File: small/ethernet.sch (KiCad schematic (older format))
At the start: 22 parts, among them J6 RJ45_Amphenol_RJMG1BD3B8K1ANR, U4 ENC28J60x-SS, Y1 Crystal

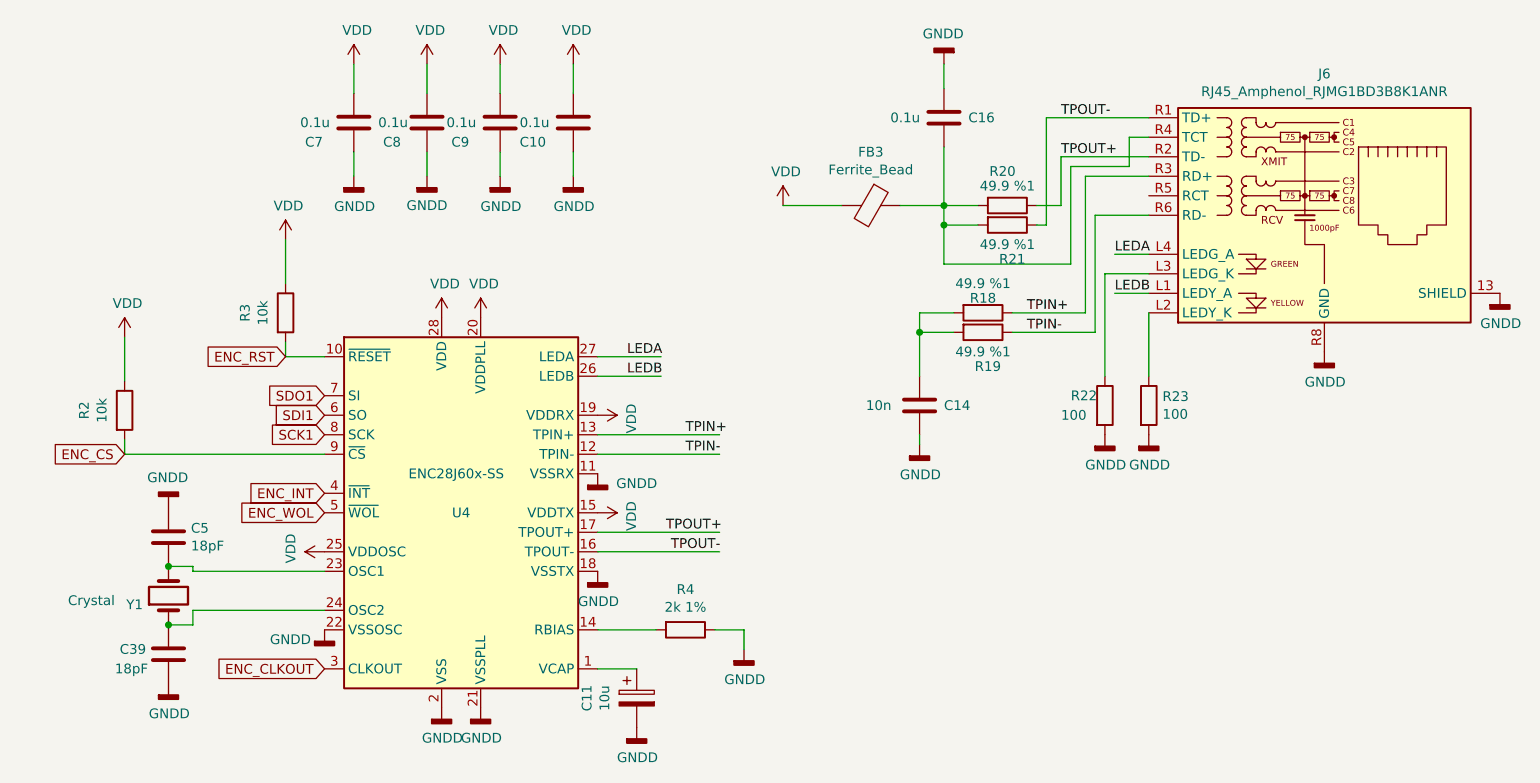
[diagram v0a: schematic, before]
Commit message: sim800 changed to sim808
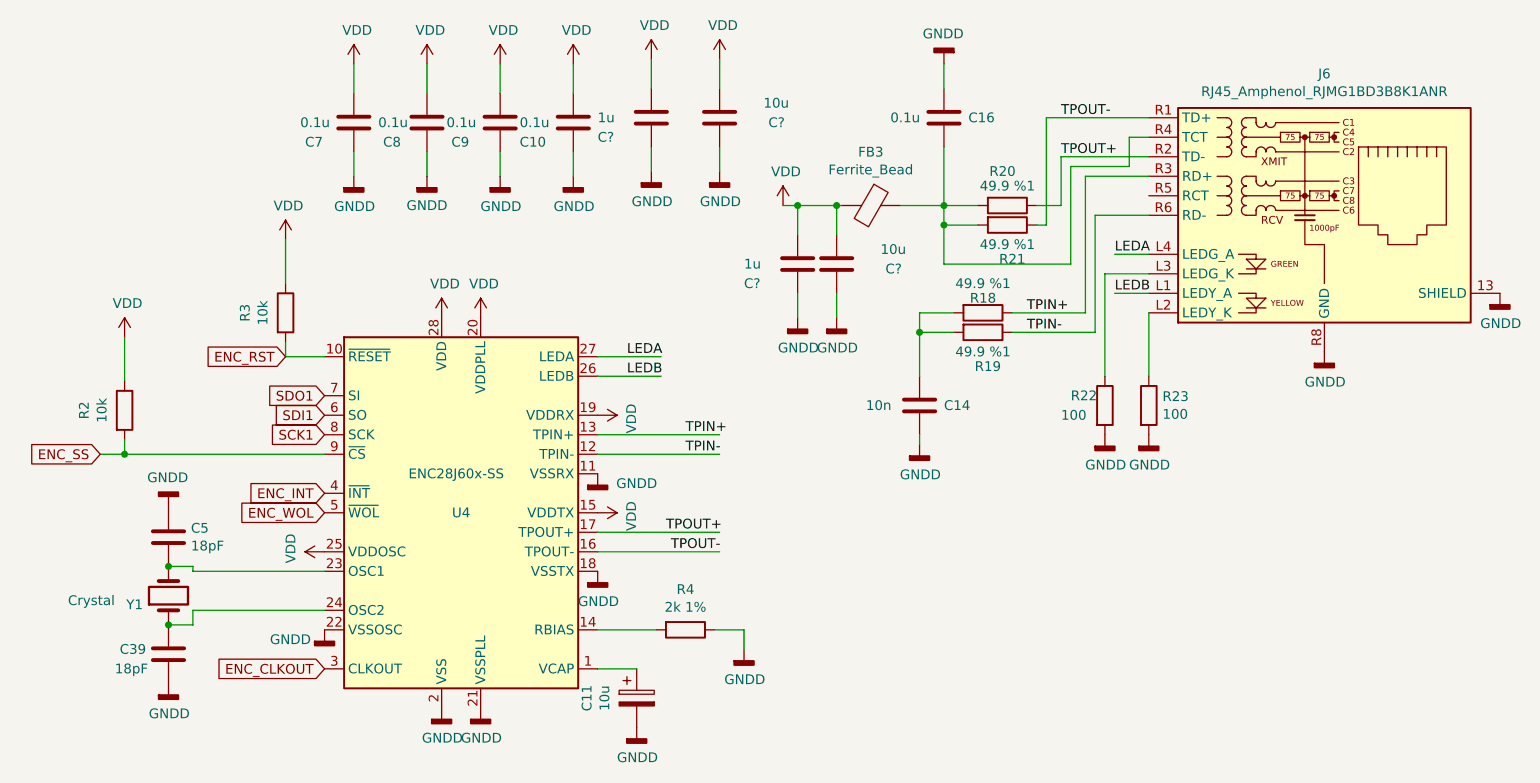
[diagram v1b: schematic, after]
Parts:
- added C? (x2): 1u, Capacitor_SMD:C_0603_1608Metric, symbol Device:C
- added C? (x2): 10u, Capacitor_SMD:C_0603_1608Metric, symbol Device:C
- R4: LCSC C22975 -> C22905; MPN 0603WAF2001T5E -> 0603WAF2321T5E
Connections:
- net labels added: ENC_SS
- net labels removed: ENC_CS
- wire segments 65 -> 76
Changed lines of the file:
@@
 $Descr A4 11693 8268
 encoding utf-8
-Sheet 6 8
+Sheet 6 9
 Title ""
 Date ""
@@
 	1    0    0    -1
 $EndComp
-Text GLabel 1625 2700 0    50   Input ~ 0
-ENC_CS
-Wire Wire Line
-	1625 2700 2650 2700
 Text GLabel 2650 2900 0    50   Input ~ 0
 ENC_INT
@@
 F 1 "2k 1%" V 4384 3600 50  0000 C CNN
 F 2 "Resistor_SMD:R_0603_1608Metric" V 4430 3600 50  0001 C CNN
-F 3 "https://datasheet.lcsc.com/szlcsc/Uniroyal-Elec-0603WAF2001T5E_C22975.pdf" H 4500 3600 50  0001 C CNN
-F 4 "C22975" V 4500 3600 50  0001 C CNN "LCSC"
-F 5 "0603WAF2001T5E" V 4500 3600 50  0001 C CNN "MPN"
+F 3 "https://datasheet.lcsc.com/szlcsc/Uniroyal-Elec-0603WAF2321T5E_C22905.pdf" H 4500 3600 50  0001 C CNN
+F 4 "C22905" V 4500 3600 50  0001 C CNN "LCSC"
+F 5 "0603WAF2321T5E" V 4500 3600 50  0001 C CNN "MPN"
 F 6 "0.0016" V 4500 3600 50  0001 C CNN "Price"
 	1    4500 3600
@@
 	1    0    0    -1
 $EndComp
-Wire Wire Line
-	5300 1425 5000 1425
 Connection ~ 5825 1525
 Wire Wire Line
@@
 $EndComp
 Connection ~ 1850 3575
+Text GLabel 1500 2700 0    50   Input ~ 0
+ENC_SS
+Wire Wire Line
+	1500 2700 1625 2700
+Connection ~ 1625 2700
+Wire Wire Line
+	1625 2700 2650 2700
+$Comp
+L power:GNDD #PWR?
+U 1 1 602BF6C6
+P 4325 1250
+AR Path="/602BF6C6" Ref="#PWR?"  Part="1"
+AR Path="/60757620/602BF6C6" Ref="#PWR?"  Part="1"
+F 0 "#PWR?" H 4325 1000 50  0001 C CNN
+F 1 "GNDD" H 4329 1095 50  0000 C CNN
+F 2 "" H 4325 1250 50  0001 C CNN
+F 3 "" H 4325 1250 50  0001 C CNN
+	1    4325 1250
+	1    0    0    -1
+$EndComp
+Wire Wire Line
+	4325 675  4325 825
+$Comp
+L power:VDD #PWR?
+U 1 1 602BF6CD
+P 4325 675
+AR Path="/602BF6CD" Ref="#PWR?"  Part="1"
+AR Path="/60757620/602BF6CD" Ref="#PWR?"  Part="1"
+F 0 "#PWR?" H 4325 525 50  0001 C CNN
+F 1 "VDD" H 4342 848 50  0000 C CNN
+F 2 "" H 4325 675 50  0001 C CNN
+F 3 "" H 4325 675 50  0001 C CNN
+	1    4325 675
+	1    0    0    -1
+$EndComp
+Wire Wire Line
+	4325 1250 4325 1125
+$Comp
+L Device:C C?
+U 1 1 602BF6D7
+P 4325 975
+AR Path="/602BF6D7" Ref="C?"  Part="1"
+AR Path="/6078415F/602BF6D7" Ref="C?"  Part="1"
+AR Path="/60757620/602BF6D7" Ref="C?"  Part="1"
+F 0 "C?" H 4050 875 50  0000 L CNN
+F 1 "1u" H 4050 975 50  0000 L CNN
+F 2 "Capacitor_SMD:C_0603_1608Metric" H 4363 825 50  0001 C CNN
+F 3 "https://datasheet.lcsc.com/szlcsc/Samsung-Electro-Mechanics-CL10A105KB8NNNC_C15849.pdf" H 4325 975 50  0001 C CNN
+F 4 "C15849" H 4325 975 50  0001 C CNN "LCSC"
+F 5 "0.0126" H 4325 975 50  0001 C CNN "Price"
+F 6 "CL10A105KB8NNNC" H 4325 975 50  0001 C CNN "MPN"
+	1    4325 975
+	1    0    0    -1
+$EndComp
+$Comp
+L power:GNDD #PWR?
+U 1 1 602C0E21
+P 4675 1250
+AR Path="/602C0E21" Ref="#PWR?"  Part="1"
+AR Path="/60757620/602C0E21" Ref="#PWR?"  Part="1"
+F 0 "#PWR?" H 4675 1000 50  0001 C CNN
+F 1 "GNDD" H 4679 1095 50  0000 C CNN
+F 2 "" H 4675 1250 50  0001 C CNN
+F 3 "" H 4675 1250 50  0001 C CNN
+	1    4675 1250
+	1    0    0    -1
+$EndComp
+Wire Wire Line
+	4675 675  4675 825
+$Comp
+L power:VDD #PWR?
+U 1 1 602C0E28
+P 4675 675
+AR Path="/602C0E28" Ref="#PWR?"  Part="1"
+AR Path="/60757620/602C0E28" Ref="#PWR?"  Part="1"
+F 0 "#PWR?" H 4675 525 50  0001 C CNN
+F 1 "VDD" H 4692 848 50  0000 C CNN
+F 2 "" H 4675 675 50  0001 C CNN
+F 3 "" H 4675 675 50  0001 C CNN
+	1    4675 675
+	1    0    0    -1
+$EndComp
+Wire Wire Line
+	4675 1250 4675 1125
+$Comp
+L Device:C C?
+U 1 1 602C0E32
+P 4675 975
+AR Path="/602C0E32" Ref="C?"  Part="1"
+AR Path="/6078415F/602C0E32" Ref="C?"  Part="1"
+AR Path="/60757620/602C0E32" Ref="C?"  Part="1"
+F 0 "C?" H 4925 950 50  0000 L CNN
+F 1 "10u" H 4900 1050 50  0000 L CNN
+F 2 "Capacitor_SMD:C_0603_1608Metric" H 4713 825 50  0001 C CNN
+F 3 "https://datasheet.lcsc.com/szlcsc/1912111437_Murata-Electronics-GRM188R61E106KA73D_C344022.pdf" H 4675 975 50  0001 C CNN
+F 4 "C344022" H 4675 975 50  0001 C CNN "LCSC"
+F 5 "0.0354" H 4675 975 50  0001 C CNN "Price"
+F 6 "GRM188R61E106KA73D" H 4675 975 50  0001 C CNN "MPN"
+	1    4675 975
+	1    0    0    -1
+$EndComp
+$Comp
+L power:GNDD #PWR?
+U 1 1 602CE763
+P 5075 2000
+AR Path="/602CE763" Ref="#PWR?"  Part="1"
+AR Path="/60757620/602CE763" Ref="#PWR?"  Part="1"
+F 0 "#PWR?" H 5075 1750 50  0001 C CNN
+F 1 "GNDD" H 5079 1845 50  0000 C CNN
+F 2 "" H 5075 2000 50  0001 C CNN
+F 3 "" H 5075 2000 50  0001 C CNN
+	1    5075 2000
+	1    0    0    -1
+$EndComp
+Wire Wire Line
+	5075 1425 5075 1575
+Wire Wire Line
+	5075 2000 5075 1875
+$Comp
+L Device:C C?
+U 1 1 602CE76E
+P 5075 1725
+AR Path="/602CE76E" Ref="C?"  Part="1"
+AR Path="/6078415F/602CE76E" Ref="C?"  Part="1"
+AR Path="/60757620/602CE76E" Ref="C?"  Part="1"
+F 0 "C?" H 4800 1625 50  0000 L CNN
+F 1 "1u" H 4800 1725 50  0000 L CNN
+F 2 "Capacitor_SMD:C_0603_1608Metric" H 5113 1575 50  0001 C CNN
+F 3 "https://datasheet.lcsc.com/szlcsc/Samsung-Electro-Mechanics-CL10A105KB8NNNC_C15849.pdf" H 5075 1725 50  0001 C CNN
+F 4 "C15849" H 5075 1725 50  0001 C CNN "LCSC"
+F 5 "0.0126" H 5075 1725 50  0001 C CNN "Price"
+F 6 "CL10A105KB8NNNC" H 5075 1725 50  0001 C CNN "MPN"
+	1    5075 1725
+	1    0    0    -1
+$EndComp
+$Comp
+L power:GNDD #PWR?
+U 1 1 602CE774
+P 5275 2000
+AR Path="/602CE774" Ref="#PWR?"  Part="1"
+AR Path="/60757620/602CE774" Ref="#PWR?"  Part="1"
+F 0 "#PWR?" H 5275 1750 50  0001 C CNN
+F 1 "GNDD" H 5279 1845 50  0000 C CNN
+F 2 "" H 5275 2000 50  0001 C CNN
+F 3 "" H 5275 2000 50  0001 C CNN
+	1    5275 2000
+	1    0    0    -1
+$EndComp
+Wire Wire Line
+	5275 1425 5275 1575
+Wire Wire Line
+	5275 2000 5275 1875
+$Comp
+L Device:C C?
+U 1 1 602CE77F
+P 5275 1725
+AR Path="/602CE77F" Ref="C?"  Part="1"
+AR Path="/6078415F/602CE77F" Ref="C?"  Part="1"
+AR Path="/60757620/602CE77F" Ref="C?"  Part="1"
+F 0 "C?" H 5525 1700 50  0000 L CNN
+F 1 "10u" H 5500 1800 50  0000 L CNN
+F 2 "Capacitor_SMD:C_0603_1608Metric" H 5313 1575 50  0001 C CNN
+F 3 "https://datasheet.lcsc.com/szlcsc/1912111437_Murata-Electronics-GRM188R61E106KA73D_C344022.pdf" H 5275 1725 50  0001 C CNN
+F 4 "C344022" H 5275 1725 50  0001 C CNN "LCSC"
+F 5 "0.0354" H 5275 1725 50  0001 C CNN "Price"
+F 6 "GRM188R61E106KA73D" H 5275 1725 50  0001 C CNN "MPN"
+	1    5275 1725
+	1    0    0    -1
+$EndComp
+Connection ~ 5075 1425
+Wire Wire Line
+	5075 1425 5000 1425
+Wire Wire Line
+	5075 1425 5275 1425
+Connection ~ 5275 1425
+Wire Wire Line
+	5275 1425 5300 1425
 $EndSCHEMATC

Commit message: simcard colder changed to 78800-0001
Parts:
- gave numbers to parts that had none: 4
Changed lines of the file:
@@
 P 4325 1250
 AR Path="/602BF6C6" Ref="#PWR?"  Part="1"
-AR Path="/60757620/602BF6C6" Ref="#PWR?"  Part="1"
-F 0 "#PWR?" H 4325 1000 50  0001 C CNN
+AR Path="/60757620/602BF6C6" Ref="#PWR0127"  Part="1"
+F 0 "#PWR0127" H 4325 1000 50  0001 C CNN
 F 1 "GNDD" H 4329 1095 50  0000 C CNN
 F 2 "" H 4325 1250 50  0001 C CNN
@@
 P 4325 675
 AR Path="/602BF6CD" Ref="#PWR?"  Part="1"
-AR Path="/60757620/602BF6CD" Ref="#PWR?"  Part="1"
-F 0 "#PWR?" H 4325 525 50  0001 C CNN
+AR Path="/60757620/602BF6CD" Ref="#PWR0130"  Part="1"
+F 0 "#PWR0130" H 4325 525 50  0001 C CNN
 F 1 "VDD" H 4342 848 50  0000 C CNN
 F 2 "" H 4325 675 50  0001 C CNN
@@
 AR Path="/602BF6D7" Ref="C?"  Part="1"
 AR Path="/6078415F/602BF6D7" Ref="C?"  Part="1"
-AR Path="/60757620/602BF6D7" Ref="C?"  Part="1"
-F 0 "C?" H 4050 875 50  0000 L CNN
+AR Path="/60757620/602BF6D7" Ref="C47"  Part="1"
+F 0 "C47" H 4050 875 50  0000 L CNN
 F 1 "1u" H 4050 975 50  0000 L CNN
 F 2 "Capacitor_SMD:C_0603_1608Metric" H 4363 825 50  0001 C CNN
@@
 P 4675 1250
 AR Path="/602C0E21" Ref="#PWR?"  Part="1"
-AR Path="/60757620/602C0E21" Ref="#PWR?"  Part="1"
-F 0 "#PWR?" H 4675 1000 50  0001 C CNN
+AR Path="/60757620/602C0E21" Ref="#PWR0135"  Part="1"
+F 0 "#PWR0135" H 4675 1000 50  0001 C CNN
 F 1 "GNDD" H 4679 1095 50  0000 C CNN
 F 2 "" H 4675 1250 50  0001 C CNN
@@
 P 4675 675
 AR Path="/602C0E28" Ref="#PWR?"  Part="1"
-AR Path="/60757620/602C0E28" Ref="#PWR?"  Part="1"
-F 0 "#PWR?" H 4675 525 50  0001 C CNN
+AR Path="/60757620/602C0E28" Ref="#PWR0136"  Part="1"
+F 0 "#PWR0136" H 4675 525 50  0001 C CNN
 F 1 "VDD" H 4692 848 50  0000 C CNN
 F 2 "" H 4675 675 50  0001 C CNN
@@
 AR Path="/602C0E32" Ref="C?"  Part="1"
 AR Path="/6078415F/602C0E32" Ref="C?"  Part="1"
-AR Path="/60757620/602C0E32" Ref="C?"  Part="1"
-F 0 "C?" H 4925 950 50  0000 L CNN
+AR Path="/60757620/602C0E32" Ref="C48"  Part="1"
+F 0 "C48" H 4925 950 50  0000 L CNN
 F 1 "10u" H 4900 1050 50  0000 L CNN
 F 2 "Capacitor_SMD:C_0603_1608Metric" H 4713 825 50  0001 C CNN
@@
 P 5075 2000
 AR Path="/602CE763" Ref="#PWR?"  Part="1"
-AR Path="/60757620/602CE763" Ref="#PWR?"  Part="1"
-F 0 "#PWR?" H 5075 1750 50  0001 C CNN
+AR Path="/60757620/602CE763" Ref="#PWR0137"  Part="1"
+F 0 "#PWR0137" H 5075 1750 50  0001 C CNN
 F 1 "GNDD" H 5079 1845 50  0000 C CNN
 F 2 "" H 5075 2000 50  0001 C CNN
@@
 AR Path="/602CE76E" Ref="C?"  Part="1"
 AR Path="/6078415F/602CE76E" Ref="C?"  Part="1"
-AR Path="/60757620/602CE76E" Ref="C?"  Part="1"
-F 0 "C?" H 4800 1625 50  0000 L CNN
+AR Path="/60757620/602CE76E" Ref="C49"  Part="1"
+F 0 "C49" H 4800 1625 50  0000 L CNN
 F 1 "1u" H 4800 1725 50  0000 L CNN
 F 2 "Capacitor_SMD:C_0603_1608Metric" H 5113 1575 50  0001 C CNN
@@
 P 5275 2000
 AR Path="/602CE774" Ref="#PWR?"  Part="1"
-AR Path="/60757620/602CE774" Ref="#PWR?"  Part="1"
-F 0 "#PWR?" H 5275 1750 50  0001 C CNN
+AR Path="/60757620/602CE774" Ref="#PWR0138"  Part="1"
+F 0 "#PWR0138" H 5275 1750 50  0001 C CNN
 F 1 "GNDD" H 5279 1845 50  0000 C CNN
 F 2 "" H 5275 2000 50  0001 C CNN
@@
 AR Path="/602CE77F" Ref="C?"  Part="1"
 AR Path="/6078415F/602CE77F" Ref="C?"  Part="1"
-AR Path="/60757620/602CE77F" Ref="C?"  Part="1"
-F 0 "C?" H 5525 1700 50  0000 L CNN
+AR Path="/60757620/602CE77F" Ref="C50"  Part="1"
+F 0 "C50" H 5525 1700 50  0000 L CNN
 F 1 "10u" H 5500 1800 50  0000 L CNN
 F 2 "Capacitor_SMD:C_0603_1608Metric" H 5313 1575 50  0001 C CNN

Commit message: BOM updated
Layout changed
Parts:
- C10, C11, C14, C16, C47, C49, C7, C8, C9, FB3: source (none) -> 0
- C39, C5: Price (none) -> 0.0073; source (none) -> 0
- C48, C50, U4: source (none) -> 1
- R18, R19, R20, R21: MPN (none) -> 0603WAF499JT5E; Price (none) -> 0.0040; source (none) -> 0
- R2, R3: MPN (none) -> 0603WAF1002T5E; source (none) -> 0
- R22, R23: MPN (none) -> 0603WAF1005T5E; source (none) -> 0
- R4: Price 0.0016 -> 0.0040; source (none) -> 1
- Y1: MPN (none) -> X322525MOB4SI; source (none) -> 0
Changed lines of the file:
@@
 F 3 "http://ww1.microchip.com/downloads/en/devicedoc/39662e.pdf" H 3350 3000 50  0001 C CNN
 F 4 " C47351" H 3350 3000 50  0001 C CNN "LCSC"
+F 5 "1" H 3350 3000 50  0001 C CNN "source"
 	1    3350 3000
 	1    0    0    -1
@@
 F 4 "C22905" V 4500 3600 50  0001 C CNN "LCSC"
 F 5 "0603WAF2321T5E" V 4500 3600 50  0001 C CNN "MPN"
-F 6 "0.0016" V 4500 3600 50  0001 C CNN "Price"
+F 6 "0.0040" V 4500 3600 50  0001 C CNN "Price"
+F 7 "1" H 4500 3600 50  0001 C CNN "source"
 	1    4500 3600
 	0    1    1    0
@@
 F 3 "https://datasheet.lcsc.com/szlcsc/Yangxing-Tech-X322525MOB4SI_C9006.pdf" H 1850 3425 50  0001 C CNN
 F 4 " C9006" V 1850 3425 50  0001 C CNN "LCSC"
+F 5 "X322525MOB4SI" H 1850 3425 50  0001 C CNN "MPN"
+F 6 "0" H 1850 3425 50  0001 C CNN "source"
 	1    1850 3425
 	0    -1   -1   0
@@
 F 4 "C1647" H 1850 3125 50  0001 C CNN "LCSC"
 F 5 "CL10C180JB8NNNC" H 1850 3125 50  0001 C CNN "MPN"
+F 6 "0.0073" H 1850 3125 50  0001 C CNN "Price"
+F 7 "0" H 1850 3125 50  0001 C CNN "source"
 	1    1850 3125
 	1    0    0    -1
@@
 F 4 " C7250" H 6650 2450 50  0001 C CNN "LCSC"
 F 5 "0.0028" H 6650 2450 50  0001 C CNN "Price"
+F 6 "0603WAF1005T5E" H 6650 2450 50  0001 C CNN "MPN"
+F 7 "0" H 6650 2450 50  0001 C CNN "source"
 	1    6650 2450
 	1    0    0    -1
@@
 F 5 "GZ2012D601TF" V 5450 1425 50  0001 C CNN "MPN"
 F 6 "0.0121" V 5450 1425 50  0001 C CNN "Price"
+F 7 "0" H 5450 1425 50  0001 C CNN "source"
 	1    5450 1425
 	0    1    1    0
@@
 F 3 "https://datasheet.lcsc.com/szlcsc/Uniroyal-Elec-0603WAF499JT5E_C23185.pdf" H 6025 2075 50  0001 C CNN
 F 4 "C23185" V 6025 2075 50  0001 C CNN "LCSC"
+F 5 "0603WAF499JT5E" H 6025 2075 50  0001 C CNN "MPN"
+F 6 "0" H 6025 2075 50  0001 C CNN "source"
+F 7 "0.0040" H 6025 2075 50  0001 C CNN "Price"
 	1    6025 2075
 	0    1    1    0
@@
 F 3 "https://datasheet.lcsc.com/szlcsc/Uniroyal-Elec-0603WAF499JT5E_C23185.pdf" H 6025 1975 50  0001 C CNN
 F 4 "C23185" V 6025 1975 50  0001 C CNN "LCSC"
+F 5 "0603WAF499JT5E" H 6025 1975 50  0001 C CNN "MPN"
+F 6 "0" H 6025 1975 50  0001 C CNN "source"
+F 7 "0.0040" H 6025 1975 50  0001 C CNN "Price"
 	1    6025 1975
 	0    1    1    0
@@
 F 3 "https://datasheet.lcsc.com/szlcsc/Uniroyal-Elec-0603WAF499JT5E_C23185.pdf" H 6150 1525 50  0001 C CNN
 F 4 "C23185" V 6150 1525 50  0001 C CNN "LCSC"
+F 5 "0603WAF499JT5E" H 6150 1525 50  0001 C CNN "MPN"
+F 6 "0" H 6150 1525 50  0001 C CNN "source"
+F 7 "0.0040" H 6150 1525 50  0001 C CNN "Price"
 	1    6150 1525
 	0    1    1    0
@@
 F 3 "https://datasheet.lcsc.com/szlcsc/Uniroyal-Elec-0603WAF499JT5E_C23185.pdf" H 6150 1425 50  0001 C CNN
 F 4 "C23185" V 6150 1425 50  0001 C CNN "LCSC"
+F 5 "0603WAF499JT5E" H 6150 1425 50  0001 C CNN "MPN"
+F 6 "0" H 6150 1425 50  0001 C CNN "source"
+F 7 "0.0040" H 6150 1425 50  0001 C CNN "Price"
 	1    6150 1425
 	0    1    1    0
@@
 F 5 "0.0071" H 2800 1000 50  0001 C CNN "Price"
 F 6 "CC0603KRX7R9BB104" H 2800 1000 50  0001 C CNN "MPN"
+F 7 "0" H 2800 1000 50  0001 C CNN "source"
 	1    2800 1000
 	1    0    0    -1
@@
 F 5 "0.0071" H 3175 1000 50  0001 C CNN "Price"
 F 6 "CC0603KRX7R9BB104" H 3175 1000 50  0001 C CNN "MPN"
+F 7 "0" H 3175 1000 50  0001 C CNN "source"
 	1    3175 1000
 	1    0    0    -1
@@
 F 5 "0.0071" H 3550 1000 50  0001 C CNN "Price"
 F 6 "CC0603KRX7R9BB104" H 3550 1000 50  0001 C CNN "MPN"
+F 7 "0" H 3550 1000 50  0001 C CNN "source"
 	1    3550 1000
 	1    0    0    -1
@@
 F 5 "0.0071" H 3925 1000 50  0001 C CNN "Price"
 F 6 "CC0603KRX7R9BB104" H 3925 1000 50  0001 C CNN "MPN"
+F 7 "0" H 3925 1000 50  0001 C CNN "source"
 	1    3925 1000
 	1    0    0    -1
@@
 F 5 "0.0071" H 5825 975 50  0001 C CNN "Price"
 F 6 "CC0603KRX7R9BB104" H 5825 975 50  0001 C CNN "MPN"
+F 7 "0" H 5825 975 50  0001 C CNN "source"
 	1    5825 975
 	1    0    0    -1
@@
 F 5 "0.0053" H 5700 2450 50  0001 C CNN "Price"
 F 6 "0603B103K500NT" H 5700 2450 50  0001 C CNN "MPN"
+F 7 "0" H 5700 2450 50  0001 C CNN "source"
 	1    5700 2450
 	1    0    0    -1
@@
 F 4 "C25804" H 1625 2475 50  0001 C CNN "LCSC"
 F 5 "0.02" H 1625 2475 50  0001 C CNN "Price"
+F 6 "0603WAF1002T5E" H 1625 2475 50  0001 C CNN "MPN"
+F 7 "0" H 1625 2475 50  0001 C CNN "source"
 	1    1625 2475
 	1    0    0    -1
@@
 F 4 "C25804" H 2450 1975 50  0001 C CNN "LCSC"
 F 5 "0.02" H 2450 1975 50  0001 C CNN "Price"
+F 6 "0603WAF1002T5E" H 2450 1975 50  0001 C CNN "MPN"
+F 7 "0" H 2450 1975 50  0001 C CNN "source"
 	1    2450 1975
 	1    0    0    -1
@@
 F 5 "TAJA106K016RNJ" H 4250 3950 50  0001 C CNN "MPN"
 F 6 "0.2135" H 4250 3950 50  0001 C CNN "Price"
+F 7 "0" H 4250 3950 50  0001 C CNN "source"
 	1    4250 3950
 	1    0    0    -1
@@
 F 4 " C7250" H 6875 2450 50  0001 C CNN "LCSC"
 F 5 "0.0028" H 6875 2450 50  0001 C CNN "Price"
+F 6 "0603WAF1005T5E" H 6875 2450 50  0001 C CNN "MPN"
+F 7 "0" H 6875 2450 50  0001 C CNN "source"
 	1    6875 2450
 	1    0    0    -1
@@
 F 4 "C1647" H 1850 3725 50  0001 C CNN "LCSC"
 F 5 "CL10C180JB8NNNC" H 1850 3725 50  0001 C CNN "MPN"
+F 6 "0.0073" H 1850 3725 50  0001 C CNN "Price"
+F 7 "0" H 1850 3725 50  0001 C CNN "source"
 	1    1850 3725
 	1    0    0    -1
@@
 F 5 "0.0126" H 4325 975 50  0001 C CNN "Price"
 F 6 "CL10A105KB8NNNC" H 4325 975 50  0001 C CNN "MPN"
+F 7 "0" H 4325 975 50  0001 C CNN "source"
 	1    4325 975
 	1    0    0    -1
@@
 F 5 "0.0354" H 4675 975 50  0001 C CNN "Price"
 F 6 "GRM188R61E106KA73D" H 4675 975 50  0001 C CNN "MPN"
+F 7 "1" H 4675 975 50  0001 C CNN "source"
 	1    4675 975
 	1    0    0    -1
@@
 F 5 "0.0126" H 5075 1725 50  0001 C CNN "Price"
 F 6 "CL10A105KB8NNNC" H 5075 1725 50  0001 C CNN "MPN"
+F 7 "0" H 5075 1725 50  0001 C CNN "source"
 	1    5075 1725
 	1    0    0    -1
@@
 F 5 "0.0354" H 5275 1725 50  0001 C CNN "Price"
 F 6 "GRM188R61E106KA73D" H 5275 1725 50  0001 C CNN "MPN"
+F 7 "1" H 5275 1725 50  0001 C CNN "source"
 	1    5275 1725
 	1    0    0    -1

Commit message: minor updates
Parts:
- Y1: Price (none) -> 0.0928
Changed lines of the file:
@@
 F 5 "X322525MOB4SI" H 1850 3425 50  0001 C CNN "MPN"
 F 6 "0" H 1850 3425 50  0001 C CNN "source"
+F 7 "0.0928" H 1850 3425 50  0001 C CNN "Price"
 	1    1850 3425
 	0    -1   -1   0
